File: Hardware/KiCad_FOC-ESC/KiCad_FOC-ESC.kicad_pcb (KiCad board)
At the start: 6 copper layers, 51 x 46 mm, 54 parts, among them IC2 TSC1801BILT, IC3 TSC1801BILT, IC4 TSC1801BILT, IC5 REF2030AIDDCR, IC6 MA702GQ-P, IC901 DRV8320SRTVR, Q1 NTTFS5D6N08XLTAG, Q2 NTTFS5D6N08XLTAG, Q3 NTTFS5D6N08XLTAG, Q4 NTTFS5D6N08XLTAG, Q5 NTTFS5D6N08XLTAG, Q6 NTTFS5D6N08XLTAG, U1 STM32G473RCTx, U3 MT6701CT, U802 ZLDO1117Q, Y1 ASDDV-16.000MHZ-LR-T

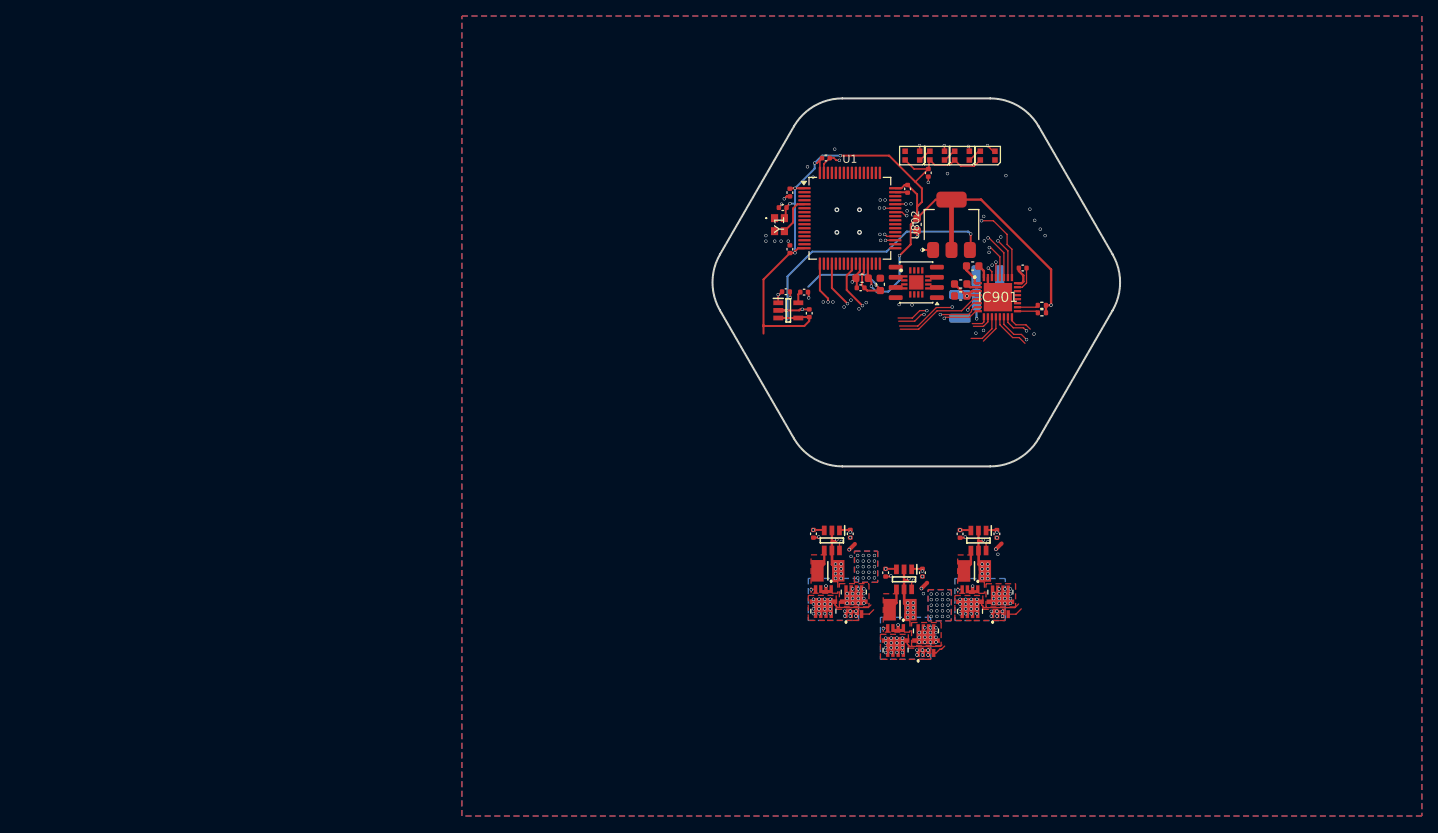
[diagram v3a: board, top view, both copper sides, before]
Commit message: rerouted FET driver
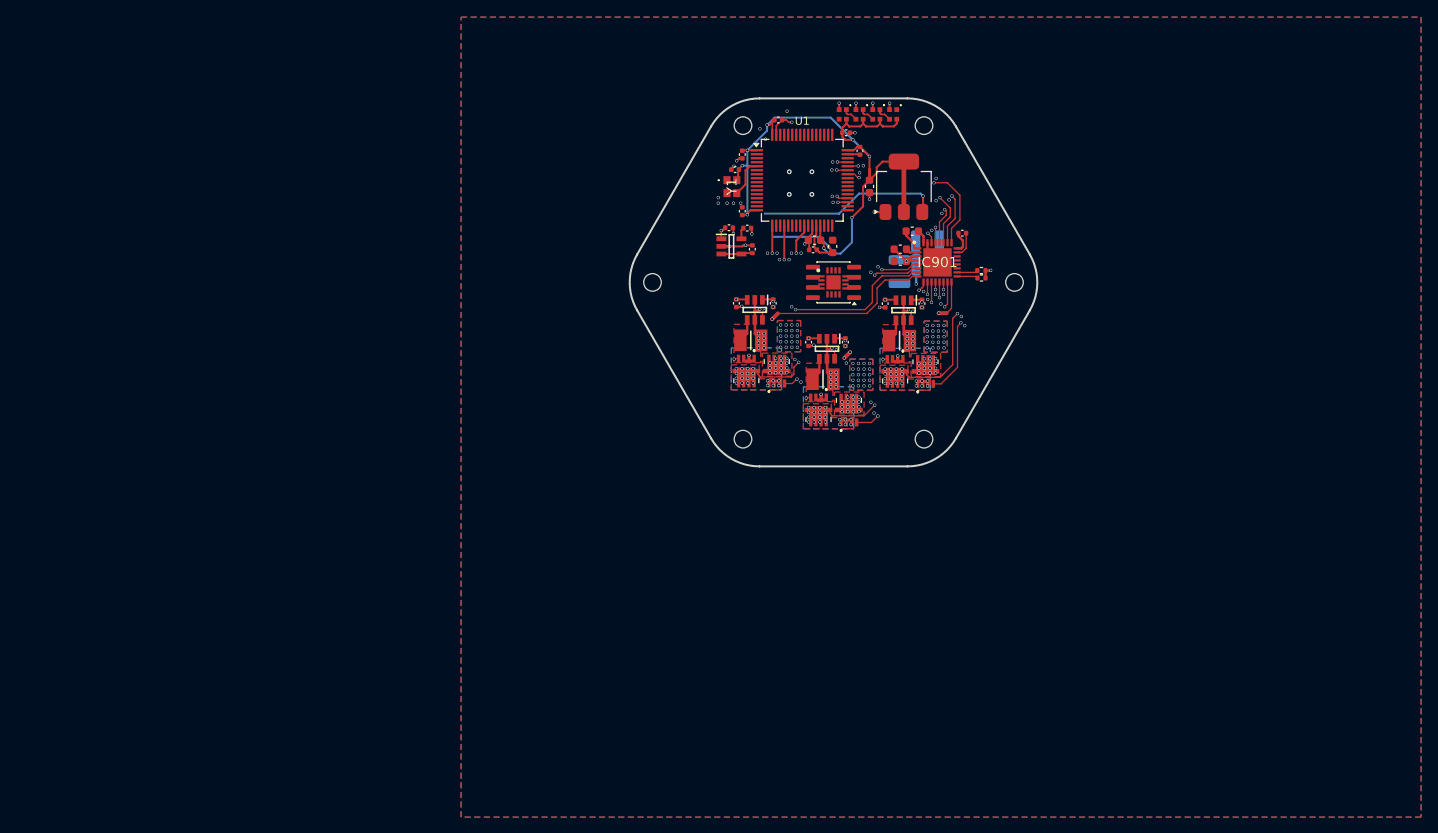
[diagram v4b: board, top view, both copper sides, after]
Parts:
- added H1: MountingHole, MountingHole:MountingHole_2.2mm_M2, F.Cu at (103.8, 83.3)
- added H2: MountingHole, MountingHole:MountingHole_2.2mm_M2, F.Cu at (115.1, 102.9)
- added H3: MountingHole, MountingHole:MountingHole_2.2mm_M2, F.Cu at (137.8, 102.9)
- added H4: MountingHole, MountingHole:MountingHole_2.2mm_M2, F.Cu at (149.1, 83.3)
- added H5: MountingHole, MountingHole:MountingHole_2.2mm_M2, F.Cu at (137.8, 63.7)
- added H6: MountingHole, MountingHole:MountingHole_2.2mm_M2, F.Cu at (115.1, 63.7)
- D1, D2, D3, D4: footprint LED_SMD:LED_WS2812B-2020_PLCC4_2.0x2.0mm -> CustomFootprintsJan:XL-1515RGBC-2812B
- moved C11 30.4 mm to (123.3, 90.8)
- moved C15 30.4 mm to (127.9, 90.8)
- moved C10 30.4 mm to (114.3, 85.9)
- moved C14 30.4 mm to (118.9, 85.9)
- moved IC2 30.4 mm to (116.6, 86.7)
- moved NT1 30.4 mm to (119.1, 87.5)
- moved NT2 30.4 mm to (128.2, 92.4)
- moved Q2 30.4 mm to (115.6, 94.3)
- moved R4 30.4 mm to (116.1, 90.5)
- moved IC3 30.4 mm to (125.6, 91.6)
- moved Q1 30.4 mm to (119.4, 94.4)
- moved Q3 30.4 mm to (128.4, 99.3)
- moved Q4 30.4 mm to (124.6, 99.2)
- moved R5 30.4 mm to (125.1, 95.4)
- moved Q5 30.3 mm to (137.9, 94.5)
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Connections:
- D1 pad 3: unconnected-(D1-DIN-Pad3) -> DebugLED_IN
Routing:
- net +3V3: track 137.6 -> 95.1 mm, vias 11 -> 12
- net GHB: track 5.41 -> 24.0 mm, vias 0 -> 2
- net SHB: track 9.57 -> 25.8 mm, vias 22 -> 24
- net GHA: track 13.0 -> 27.4 mm, vias 0 -> 2
- net SHA: track 16.6 -> 30.6 mm
- net GLB: track 11.8 -> 24.4 mm, vias 2 -> 3
- net VCC: track 24.9 -> 13.0 mm
- net GLA: track 19.8 -> 31.1 mm, vias 4 -> 2
- net /FETs/DRV8320S_1/SPB: track 2.18 -> 13.1 mm, vias 0 -> 2
- net OUT3: track 15.6 -> 26.5 mm
- net +5V: track 32.8 -> 23.0 mm
- net SHC: track 9.92 -> 19.5 mm, vias 23 -> 24
- net GHC: track 7.01 -> 16.4 mm, vias 0 -> 2
- net /FETs/DRV8320S_1/SPA: track 11.6 -> 20.5 mm, vias 2 -> 0
- net +1V5: track 15.5 -> 6.65 mm
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
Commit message: edited routs
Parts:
- removed H2, H3: MountingHole, MountingHole:MountingHole_2.2mm_M2
- added NT4: NetTie_2, NetTie:NetTie-2_SMD_Pad0.5mm, F.Cu at (114.9, 94.9)
- added NT5: NetTie_2, NetTie:NetTie-2_SMD_Pad0.5mm, F.Cu at (125.5, 94.9)
- added NT6: NetTie_2, NetTie:NetTie-2_SMD_Pad0.5mm, F.Cu at (136.1, 94.9)
- moved NT3 9.42 mm to (139.0, 96.5), turned to -135 degrees
- moved NT1 9.29 mm to (118.0, 96.7)
- moved Q1 6.22 mm to (117.6, 100.4)
- moved C10 6.22 mm to (112.6, 91.9)
- moved C14 6.22 mm to (117.2, 91.9)
- moved IC2 6.22 mm to (114.9, 92.7)
- moved Q2 6.22 mm to (113.8, 100.3)
- moved R4 6.22 mm to (114.4, 96.5)
- moved Q5 5.98 mm to (138.8, 100.4)
- moved IC4 5.98 mm to (136.1, 92.7)
- moved Q6 5.98 mm to (135.0, 100.3)
- moved R6 5.98 mm to (135.6, 96.5)
- moved C16 5.98 mm to (138.4, 91.9)
- moved C12 5.98 mm to (133.8, 91.9)
- moved NT2 4.12 mm to (128.2, 96.5)
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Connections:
- IC2 pad 5: GND -> Net-(IC2-IN-)
- IC3 pad 5: GND -> Net-(IC3-IN-)
- IC4 pad 5: GND -> Net-(IC4-IN-)
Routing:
- net +3V3: track 95.1 -> 140.0 mm, vias 12 -> 14
- net +1V5: track 6.65 -> 41.5 mm, vias 4 -> 3
- net GND: track 49.9 -> 36.0 mm, vias 151 -> 103
- net GHA: track 27.4 -> 40.7 mm
- net /FETs/DRV8320S_1/SPC: track 4.15 -> 13.7 mm
- net /FETs/DRV8320S_1/SPA: track 20.5 -> 29.9 mm
- net SHA: track 30.6 -> 38.8 mm
- net GLA: track 31.1 -> 38.9 mm
- net OUT1: track 12.3 -> 19.0 mm
- net GHC: track 16.4 -> 22.5 mm
- net SLC: track 13.0 -> 7.11 mm
- net OUT3: track 26.5 -> 31.9 mm
- net GLC: track 16.8 -> 22.1 mm
- net /FETs/DRV8320S_1/SPB: track 13.1 -> 18.0 mm, vias 2 -> 0
- net +3V: track 15.3 -> 20.1 mm, vias 1 -> 2
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- added copper zone on B.Cu, net VCC
- removed copper zone on F.Cu, net SLA
- removed copper zone on F.Cu, net SLB
- removed copper zone on F.Cu, net SLC
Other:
- board text added: "F.Cu GND IN1 GND IN2 VCC only FETs IN3 GND IN4 VCC only FETs B.Cu GND"

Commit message: general routing, edited: Software inputs (#19)
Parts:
- added C18: 100nF, Capacitor_SMD:C_0402_1005Metric, F.Cu at (96.8, 66.4)
- added C20: 100nF, Capacitor_SMD:C_0402_1005Metric, F.Cu at (127.8, 76.5)
- added C21: 4.7nF, Capacitor_SMD:C_0402_1005Metric, F.Cu at (152.4, 55.0)
- added IC1: TCAN3414DDFR, SamacSys_Parts:INA190A2NDDFREP, F.Cu at (144.6, 54.6)
- added J1: Conn_01x06, SamacSys_Parts:SM04B-GHS-TB, F.Cu at (156.8, 56.2)
- added J2: Prog, SamacSys_Parts:SM06B-GHS-TB, F.Cu at (108.4, 70.2)
- added R1: 10k, Resistor_SMD:R_0603_1608Metric, F.Cu at (102.4, 67.3)
- added R2: 60, Resistor_SMD:R_0603_1608Metric, F.Cu at (150.8, 53.5)
- added R3: 60, Resistor_SMD:R_0603_1608Metric, F.Cu at (150.8, 56.5)
- U802: moved to B.Cu
- moved U802 13.4 mm to (121.9, 70.9)
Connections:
- U1 pad 49: unconnected-(U1-PA13-Pad49) -> SWDIO
- U1 pad 50: unconnected-(U1-PA14-Pad50) -> SWCLK
- U1 pad 56: unconnected-(U1-PB3-Pad56) -> SWO
- U1 pad 57: unconnected-(U1-PB4-Pad57) -> CAN_STB
- U1 pad 58: unconnected-(U1-PB5-Pad58) -> CAN_SHDNVIO
- U1 pad 7: unconnected-(U1-PG10-Pad7) -> NRST
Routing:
- net SWCLK: track 0.00 -> 25.0 mm, vias 0 -> 2
- net SWDIO: track 0.00 -> 24.5 mm, vias 0 -> 2
- net +5V: track 23.0 -> 0.00 mm, vias 1 -> 0
- net +3V3: track 140.0 -> 162.9 mm
- net +1V5: track 41.5 -> 57.4 mm, vias 3 -> 5
- net CANL: track 0.00 -> 12.4 mm
- net CANH: track 0.00 -> 12.2 mm
- net +3V: track 20.1 -> 8.28 mm
- net INLB: track 21.1 -> 18.6 mm
- net Net-(C21-Pad1): track 0.00 -> 2.48 mm
- net INHC: track 21.2 -> 23.0 mm
- net INLA: track 23.8 -> 22.5 mm
- net INHB: track 22.3 -> 21.0 mm
- net INHA: track 21.5 -> 20.6 mm
- net INLC: track 16.6 -> 16.0 mm
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- added copper zone on F.Cu, net SLA
- added copper zone on F.Cu, net SLB
- added copper zone on F.Cu, net SLC
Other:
- board text added: "SPI and CANBUS"
- board text added: "VBAT Balancing stecker"

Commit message: routing
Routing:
- net SWO: track 0.00 -> 23.6 mm, vias 1 -> 2
- net NRST: track 0.00 -> 17.2 mm, vias 1 -> 2
